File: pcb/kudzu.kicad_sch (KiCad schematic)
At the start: 0 parts

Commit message: pcb: Update schematic to WIP6
Change-Id: I9e9f727ad2774ee986f2f97450dc509901129aec
Reviewed-on: https://pigweed-review.googlesource.com/c/pigweed/kudzu/+/169650
Reviewed-by: Anthony DiGirolamo <tonymd@google.com>
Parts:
- added R24, R25, R26, R27, R28, R29, R30, R31: 0, symbol Device:R_Small
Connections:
- new net +3V3: R24.2, R26.2, R28.2, R30.2
- new net BOARD_ID0: R24.1, R25.2
- new net BOARD_ID1: R26.1, R27.2
- new net BOARD_ID2: R28.1, R29.2
- new net BOARD_ID3: R30.1, R31.2
- new net GND: R25.1, R27.1, R29.1, R31.1

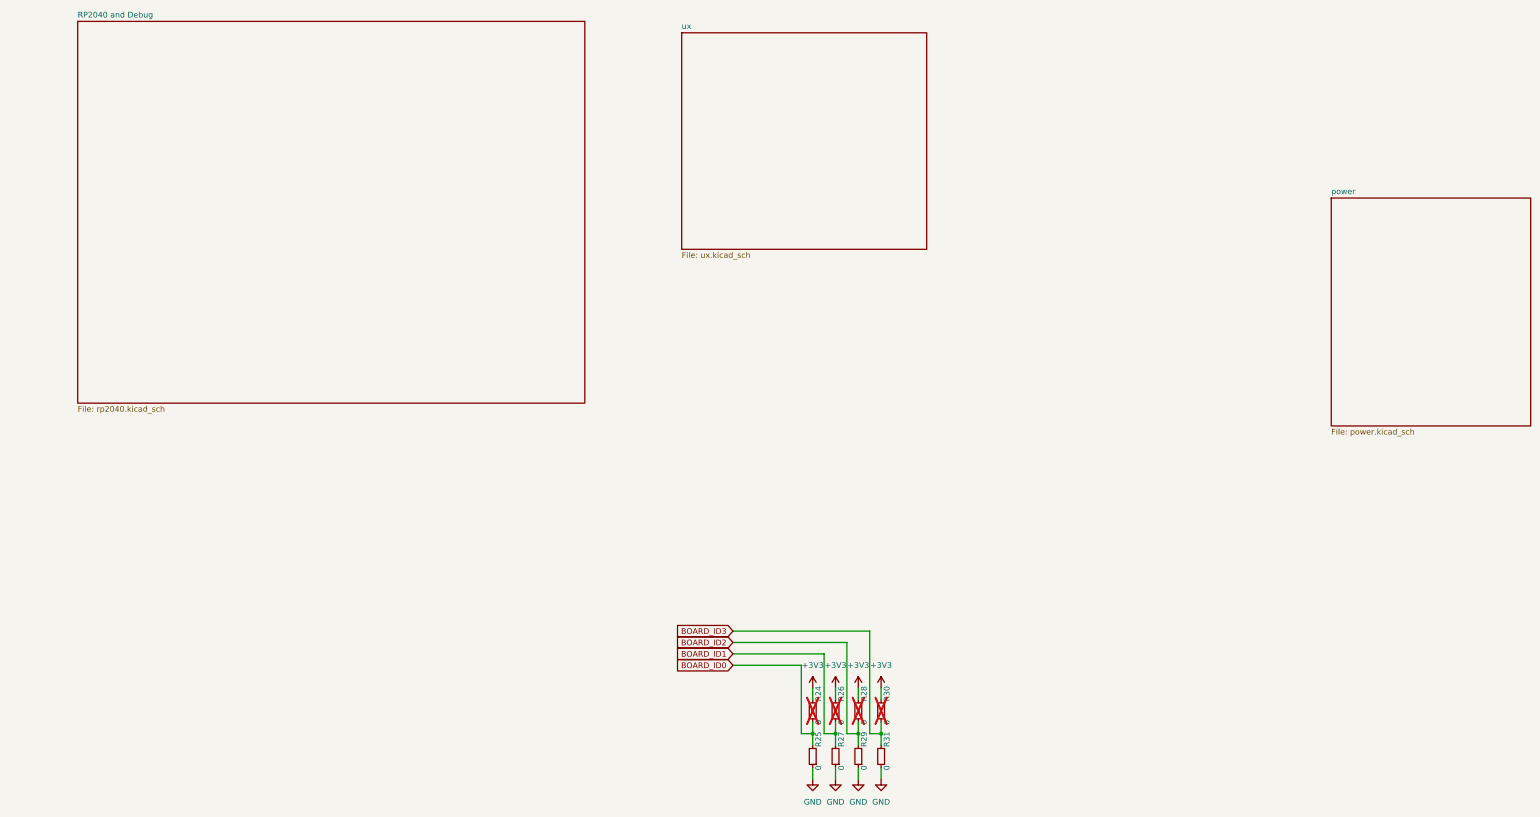
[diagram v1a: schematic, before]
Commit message: pcb: Update pcb to WIP7
Changes:

- Pruned unused parts from `kudzu-parts.kicad_sym`.
- Updated all parts in `kudzu-parts.kicad_sym` to pass `klc-check/check_symbol.py`.
- Switched to `PI4IOE5V6416` IO expander which has programmable pull-up.
- Removed pull-ups on `BOARD_ID*`, `BUTTON_*`, `TOUCH_RESET`, and `DISP_RESET`
  in favor of internal pull-ups in the IO expander.
- Added pull-up to `RESET_N`.
- Removed test points from `QSPI_*`.
- Switched to QFN version of `MCP73831`.
- Fixed missing pin number on `MAX17048` `QSTRT`.
- Removed pull-up on 3.3V regulator's `EN` pin and tied directly to `VIN`.
- Added extra decoupling caps to rp2040's 3.3V and 1.1V lines per design guide.
- Added note to add axis diagram to silk screen on board.
- Miscellaneous visual cleanup.
- Added FET on conduction path for system power.
- Added circuit to charge at 250mA when system is on and 500mA when system is off.
- Assigned all RP2040 IOs.
- Created and switched to dedicated symbols for DPAD, A/B, and SELECT/START.
- Switched display connector symbol for one with a mounting pin.
- Set test point values to net names.
- Selected LEDs and current limiting resistor values.
- Added closed solder jumpers to GBA Link signals.
- Changed solder jumper on GBA VCC pin to open.
- Changed LCD decoupling to mach reference circuit.
- Connected DISP_RD (J9 Pin 12) to +3V3.
- Connected DB0-15 (J9 Pins 17-32) to GND.
- Updated 12MHz Crystal (Y1) to correct symbol and foot print.

Change-Id: I6d0fe442c50df116031305f5165b6a29d3572d45
Reviewed-on: https://pigweed-review.googlesource.com/c/pigweed/kudzu/+/169858
Reviewed-by: Anthony DiGirolamo <tonymd@google.com>
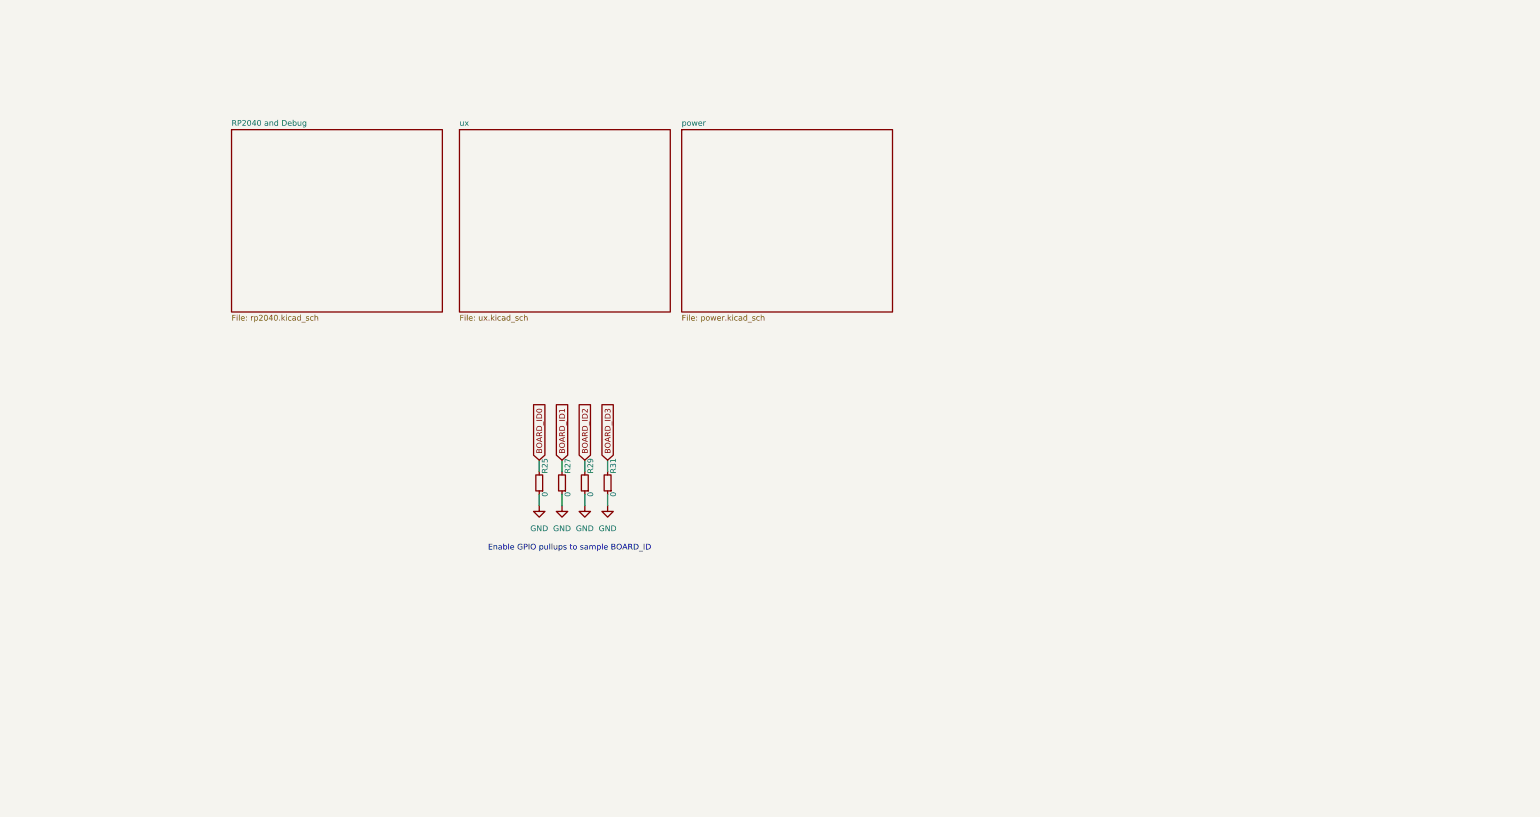
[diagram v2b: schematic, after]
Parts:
- removed R24, R26, R28, R30: 0, symbol Device:R_Small
- R25, R27, R29, R31: footprint (none) -> Resistor_SMD:R_0603_1608Metric
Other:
- note added: "Enable GPIO pullups to sample BOARD_ID"
- moved on the sheet: R25, R27, R29, R31

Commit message: pcb: rev 0-r1 - board routed
Change-Id: Icb9c0ddbcf21cc7f2bac7bbcd371ff5a97baf35d
Reviewed-on: https://pigweed-review.googlesource.com/c/pigweed/kudzu/+/170233
Reviewed-by: Anthony DiGirolamo <tonymd@google.com>
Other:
- company: (none) -> Copyright 2023 The Pigweed Authors
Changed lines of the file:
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@@
   (title_block
     (title "Kudzu")
-    (date "2023-09-07")
-    (rev "WIP7")
+    (date "2023-09-12")
+    (rev "rev0-rc1")
+    (company "Copyright 2023 The Pigweed Authors")
   )
   (wire (pts (xy 147.32 130.81) (xy 147.32 133.35))

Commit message: pcb: Rev 0 ready for fab!
Change-Id: Ie6eacb65a214d2b5a2b9a0c8f76846194f090e28
Reviewed-on: https://pigweed-review.googlesource.com/c/pigweed/kudzu/+/170857
Reviewed-by: Anthony DiGirolamo <tonymd@google.com>
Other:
- added sheet misc (misc.kicad_sch)
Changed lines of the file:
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@@
   (title_block
     (title "Kudzu")
-    (date "2023-09-12")
-    (rev "0-rc2")
+    (date "2023-09-13")
+    (rev "0")
     (company "Copyright 2023 The Pigweed Authors")
   )
@@
       )
     )
+  )
+  (sheet (at 13.97 173.99) (size 25.4 25.4) (fields_autoplaced)
+    (stroke (width 0.1524) (type solid))
+    (fill (color 0 0 0 0.0000))
+    (property "Sheetname" "misc" (at 13.97 173.2784 0)
+      (effects (font (size 1.27 1.27)) (justify left bottom))
+    )
+    (property "Sheetfile" "misc.kicad_sch" (at 13.97 199.9746 0)
+      (effects (font (size 1.27 1.27)) (justify left top))
+    )
+    (instances
+      (project "kudzu"
+        (path "/30e30bdf-50e5-46a8-92c7-0e280cceabe8" (page "5"))
+      )
+    )

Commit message: pcb: Add part numbers for passives
Change-Id: Ie1730dd2a7126b7f6f602689064a4dbf8996e7b6
Reviewed-on: https://pigweed-review.googlesource.com/c/pigweed/kudzu/+/172895
Reviewed-by: Anthony DiGirolamo <anthony.digirolamo@gmail.com>
Reviewed-by: Anthony DiGirolamo <tonymd@google.com>
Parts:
- R25, R27, R29, R31: DigiKey PN (none) -> 13-AC0402FR-070RLTR-ND; Price @ 10 (none) -> 0.01320; Price @ 25 (none) -> 0.01000
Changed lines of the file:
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@@
       (effects (font (size 1.27 1.27)) hide)
     )
-    (property "Price @ 10" "" (at 132.08 135.89 0)
+    (property "Price @ 10" "0.01320" (at 132.08 135.89 0)
       (effects (font (size 1.27 1.27)) hide)
     )
-    (property "Price @ 25" "" (at 132.08 135.89 0)
+    (property "Price @ 25" "0.01000" (at 132.08 135.89 0)
+      (effects (font (size 1.27 1.27)) hide)
+    )
+    (property "DigiKey PN" "13-AC0402FR-070RLTR-ND" (at 132.08 135.89 0)
       (effects (font (size 1.27 1.27)) hide)
     )
@@
       (effects (font (size 1.27 1.27)) hide)
     )
-    (property "Price @ 10" "" (at 142.24 135.89 0)
+    (property "Price @ 10" "0.01320" (at 142.24 135.89 0)
       (effects (font (size 1.27 1.27)) hide)
     )
-    (property "Price @ 25" "" (at 142.24 135.89 0)
+    (property "Price @ 25" "0.01000" (at 142.24 135.89 0)
+      (effects (font (size 1.27 1.27)) hide)
+    )
+    (property "DigiKey PN" "13-AC0402FR-070RLTR-ND" (at 142.24 135.89 0)
       (effects (font (size 1.27 1.27)) hide)
     )
@@
       (effects (font (size 1.27 1.27)) hide)
     )
-    (property "Price @ 10" "" (at 147.32 135.89 0)
+    (property "Price @ 10" "0.01320" (at 147.32 135.89 0)
       (effects (font (size 1.27 1.27)) hide)
     )
-    (property "Price @ 25" "" (at 147.32 135.89 0)
+    (property "Price @ 25" "0.01000" (at 147.32 135.89 0)
+      (effects (font (size 1.27 1.27)) hide)
+    )
+    (property "DigiKey PN" "13-AC0402FR-070RLTR-ND" (at 147.32 135.89 0)
       (effects (font (size 1.27 1.27)) hide)
     )
@@
       (effects (font (size 1.27 1.27)) hide)
     )
-    (property "Price @ 10" "" (at 137.16 135.89 0)
+    (property "Price @ 10" "0.01320" (at 137.16 135.89 0)
       (effects (font (size 1.27 1.27)) hide)
     )
-    (property "Price @ 25" "" (at 137.16 135.89 0)
+    (property "Price @ 25" "0.01000" (at 137.16 135.89 0)
       (effects (font (size 1.27 1.27)) hide)
     )
+    (property "DigiKey PN" "13-AC0402FR-070RLTR-ND" (at 137.16 135.89 0)
+      (effects (font (size 1.27 1.27)) hide)
+    )
